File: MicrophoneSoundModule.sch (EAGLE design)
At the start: 23 parts, among them IC1 TLC272 TSSOP8

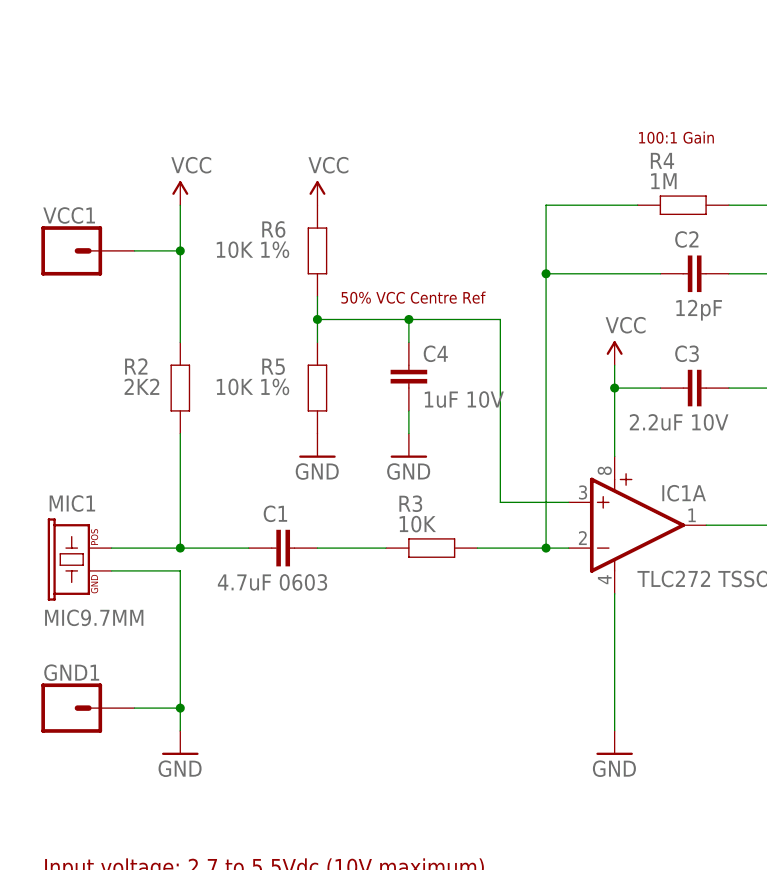
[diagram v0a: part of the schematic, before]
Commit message: Reorient AC decoupling capacitors to reduce noise
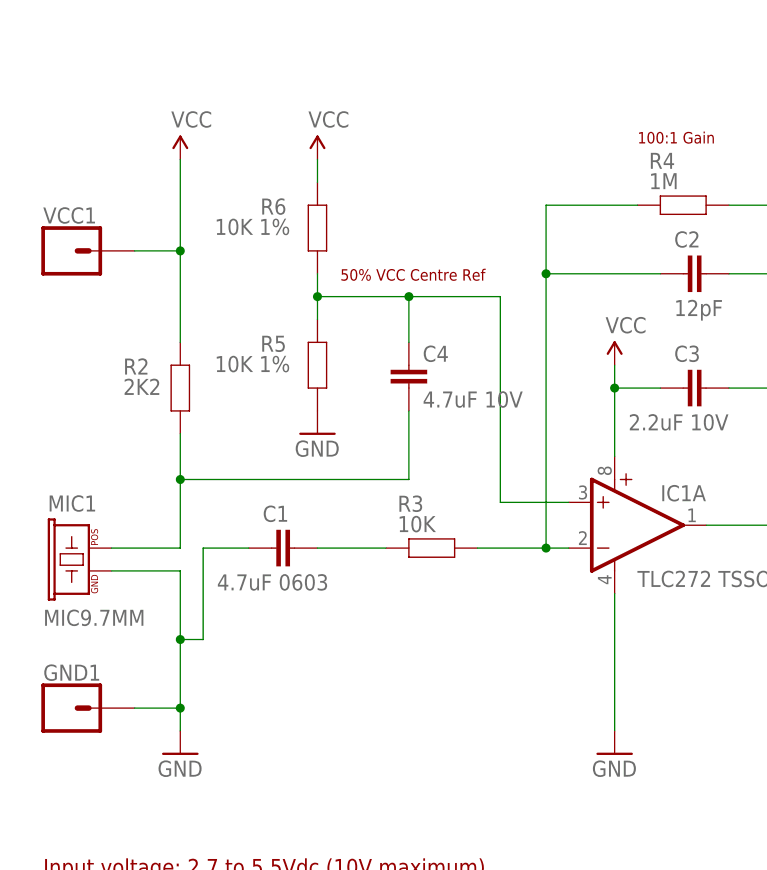
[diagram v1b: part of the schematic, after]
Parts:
- C4: value 1uF 10V -> 4.7uF 10V
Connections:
- net GND: now also C1.1; no longer C4.1
- net N$2: now also C4.1; no longer C1.1
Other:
- moved on the sheet: R5, R6
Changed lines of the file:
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@@
 <part name="R6" library="freetronics-master-v1" deviceset="RESISTOR" device="0603" value="10K 1%"/>
 <part name="P+4" library="freetronics-marc" deviceset="VCC" device=""/>
-<part name="C4" library="freetronics-master-v1" deviceset="CAP" device="0603" value="1uF 10V"/>
-<part name="GND8" library="freetronics" deviceset="GND" device=""/>
+<part name="C4" library="freetronics-master-v1" deviceset="CAP" device="0603" value="4.7uF 10V"/>
 <part name="C5" library="freetronics-master-v1" deviceset="CAP" device="0603" value="100nF"/>
 <part name="R8" library="freetronics-master-v1" deviceset="RESISTOR" device="0603" value="100K"/>
@@
 <text x="68.326" y="14.478" size="1.778" layer="94">www.freetronics.com/mic</text>
 <text x="10.16" y="27.178" size="1.778" layer="94">Input voltage: 2.7 to 5.5Vdc (10V maximum)</text>
-<text x="43.18" y="90.678" size="1.27" layer="94">50% VCC Centre Ref</text>
+<text x="43.18" y="93.218" size="1.27" layer="94">50% VCC Centre Ref</text>
 <text x="76.2" y="108.458" size="1.27" layer="94">100:1 Gain</text>
 <text x="93.98" y="119.888" size="1.6764" layer="94" ratio="10">MIC Output Pin is centred at approx 50% of VCC with no sound</text>
@@
 <attribute name="VALUE" x="80.264" y="89.281" size="1.778" layer="96"/>
 </instance>
-<instance part="P+2" gate="1" x="25.4" y="101.6"/>
+<instance part="P+2" gate="1" x="25.4" y="106.68"/>
 <instance part="C3" gate="G$1" x="83.82" y="81.28" smashed="yes" rot="R90">
 <attribute name="NAME" x="80.264" y="84.201" size="1.778" layer="95"/>
@@
 <instance part="P+3" gate="1" x="73.66" y="83.82"/>
 <instance part="GND3" gate="1" x="73.66" y="40.64"/>
-<instance part="GND4" gate="1" x="40.64" y="73.66"/>
+<instance part="GND4" gate="1" x="40.64" y="76.2"/>
 <instance part="GND6" gate="1" x="93.98" y="78.74"/>
 <instance part="GND7" gate="1" x="25.4" y="40.64"/>
-<instance part="R5" gate="G$1" x="40.64" y="81.28" smashed="yes" rot="R90">
-<attribute name="NAME" x="34.29" y="82.7786" size="1.778" layer="95"/>
-<attribute name="VALUE" x="29.21" y="80.518" size="1.778" layer="96"/>
-</instance>
-<instance part="R6" gate="G$1" x="40.64" y="96.52" smashed="yes" rot="R90">
-<attribute name="NAME" x="34.29" y="98.0186" size="1.778" layer="95"/>
-<attribute name="VALUE" x="29.21" y="95.758" size="1.778" layer="96"/>
-</instance>
-<instance part="P+4" gate="1" x="40.64" y="101.6"/>
+<instance part="R5" gate="G$1" x="40.64" y="83.82" smashed="yes" rot="R90">
+<attribute name="NAME" x="34.29" y="85.3186" size="1.778" layer="95"/>
+<attribute name="VALUE" x="29.21" y="83.058" size="1.778" layer="96"/>
+</instance>
+<instance part="R6" gate="G$1" x="40.64" y="99.06" smashed="yes" rot="R90">
+<attribute name="NAME" x="34.29" y="100.5586" size="1.778" layer="95"/>
+<attribute name="VALUE" x="29.21" y="98.298" size="1.778" layer="96"/>
+</instance>
+<instance part="P+4" gate="1" x="40.64" y="106.68"/>
 <instance part="C4" gate="G$1" x="50.8" y="83.82" smashed="yes" rot="R180">
 <attribute name="NAME" x="52.324" y="84.201" size="1.778" layer="95"/>
 <attribute name="VALUE" x="52.324" y="79.121" size="1.778" layer="96"/>
 </instance>
-<instance part="GND8" gate="1" x="50.8" y="73.66"/>
 <instance part="C5" gate="G$1" x="109.22" y="66.04" smashed="yes" rot="R90">
 <attribute name="NAME" x="105.664" y="68.961" size="1.778" layer="95"/>
@@
 <segment>
 <wire x1="17.78" y1="60.96" x2="25.4" y2="60.96" width="0.1524" layer="91"/>
-<wire x1="25.4" y1="60.96" x2="25.4" y2="45.72" width="0.1524" layer="91"/>
+<wire x1="25.4" y1="60.96" x2="25.4" y2="53.34" width="0.1524" layer="91"/>
+<wire x1="25.4" y1="53.34" x2="25.4" y2="45.72" width="0.1524" layer="91"/>
 <wire x1="25.4" y1="45.72" x2="25.4" y2="43.18" width="0.1524" layer="91"/>
 <wire x1="20.32" y1="45.72" x2="25.4" y2="45.72" width="0.1524" layer="91"/>
@@
 <pinref part="GND7" gate="1" pin="GND"/>
 <pinref part="GND1" gate="G$1" pin="1"/>
+<pinref part="C1" gate="G$1" pin="1"/>
+<wire x1="33.02" y1="63.5" x2="27.94" y2="63.5" width="0.1524" layer="91"/>
+<wire x1="27.94" y1="63.5" x2="27.94" y2="53.34" width="0.1524" layer="91"/>
+<wire x1="27.94" y1="53.34" x2="25.4" y2="53.34" width="0.1524" layer="91"/>
+<junction x="25.4" y="53.34"/>
 </segment>
 <segment>
 <pinref part="GND4" gate="1" pin="GND"/>
 <pinref part="R5" gate="G$1" pin="1"/>
-</segment>
-<segment>
-<wire x1="50.8" y1="78.74" x2="50.8" y2="76.2" width="0.1524" layer="91"/>
-<pinref part="C4" gate="G$1" pin="1"/>
-<pinref part="GND8" gate="1" pin="GND"/>
 </segment>
 <segment>
@@
 <net name="VCC" class="0">
 <segment>
-<wire x1="25.4" y1="101.6" x2="25.4" y2="96.52" width="0.1524" layer="91"/>
+<wire x1="25.4" y1="106.68" x2="25.4" y2="96.52" width="0.1524" layer="91"/>
 <wire x1="25.4" y1="96.52" x2="25.4" y2="86.36" width="0.1524" layer="91"/>
 <wire x1="20.32" y1="96.52" x2="25.4" y2="96.52" width="0.1524" layer="91"/>
@@
 </segment>
 <segment>
-<pinref part="R6" gate="G$1" pin="2"/>
-<pinref part="P+4" gate="1" pin="VCC"/>
-</segment>
-<segment>
 <wire x1="124.46" y1="78.74" x2="124.46" y2="81.28" width="0.1524" layer="91"/>
 <pinref part="R7" gate="G$1" pin="2"/>
 <pinref part="P+5" gate="1" pin="VCC"/>
 </segment>
+<segment>
+<pinref part="P+4" gate="1" pin="VCC"/>
+<pinref part="R6" gate="G$1" pin="2"/>
+<wire x1="40.64" y1="106.68" x2="40.64" y2="104.14" width="0.1524" layer="91"/>
+</segment>
 </net>
 <net name="N$1" class="0">
@@
 <segment>
 <wire x1="17.78" y1="63.5" x2="25.4" y2="63.5" width="0.1524" layer="91"/>
-<wire x1="25.4" y1="63.5" x2="33.02" y2="63.5" width="0.1524" layer="91"/>
-<wire x1="25.4" y1="76.2" x2="25.4" y2="63.5" width="0.1524" layer="91"/>
-<junction x="25.4" y="63.5"/>
+<wire x1="25.4" y1="76.2" x2="25.4" y2="71.12" width="0.1524" layer="91"/>
 <pinref part="MIC1" gate="G$1" pin="POS"/>
-<pinref part="C1" gate="G$1" pin="1"/>
 <pinref part="R2" gate="G$1" pin="1"/>
+<pinref part="C4" gate="G$1" pin="1"/>
+<wire x1="25.4" y1="71.12" x2="25.4" y2="63.5" width="0.1524" layer="91"/>
+<wire x1="50.8" y1="78.74" x2="50.8" y2="71.12" width="0.1524" layer="91"/>
+<wire x1="50.8" y1="71.12" x2="25.4" y2="71.12" width="0.1524" layer="91"/>
+<junction x="25.4" y="71.12"/>
 </segment>
 </net>
@@
 </segment>
 </net>
-<net name="N$5" class="0">
-<segment>
-<wire x1="40.64" y1="91.44" x2="40.64" y2="88.9" width="0.1524" layer="91"/>
-<wire x1="40.64" y1="88.9" x2="40.64" y2="86.36" width="0.1524" layer="91"/>
-<wire x1="50.8" y1="86.36" x2="50.8" y2="88.9" width="0.1524" layer="91"/>
-<wire x1="50.8" y1="88.9" x2="40.64" y2="88.9" width="0.1524" layer="91"/>
-<wire x1="50.8" y1="88.9" x2="60.96" y2="88.9" width="0.1524" layer="91"/>
-<wire x1="60.96" y1="88.9" x2="60.96" y2="68.58" width="0.1524" layer="91"/>
-<wire x1="60.96" y1="68.58" x2="68.58" y2="68.58" width="0.1524" layer="91"/>
-<junction x="40.64" y="88.9"/>
-<junction x="50.8" y="88.9"/>
-<pinref part="R6" gate="G$1" pin="1"/>
-<pinref part="R5" gate="G$1" pin="2"/>
-<pinref part="C4" gate="G$1" pin="2"/>
-<pinref part="IC1" gate="A" pin="+IN"/>
-</segment>
-</net>
 <net name="N$7" class="0">
 <segment>
@@
 </segment>
 </net>
+<net name="N$8" class="0">
+<segment>
+<pinref part="R6" gate="G$1" pin="1"/>
+<wire x1="40.64" y1="93.98" x2="40.64" y2="91.44" width="0.1524" layer="91"/>
+<pinref part="R5" gate="G$1" pin="2"/>
+<wire x1="40.64" y1="91.44" x2="40.64" y2="88.9" width="0.1524" layer="91"/>
+<wire x1="40.64" y1="91.44" x2="50.8" y2="91.44" width="0.1524" layer="91"/>
+<pinref part="C4" gate="G$1" pin="2"/>
+<wire x1="50.8" y1="91.44" x2="50.8" y2="86.36" width="0.1524" layer="91"/>
+<wire x1="50.8" y1="91.44" x2="60.96" y2="91.44" width="0.1524" layer="91"/>
+<wire x1="60.96" y1="91.44" x2="60.96" y2="68.58" width="0.1524" layer="91"/>
+<wire x1="60.96" y1="68.58" x2="68.58" y2="68.58" width="0.1524" layer="91"/>
+<pinref part="IC1" gate="A" pin="+IN"/>
+<junction x="50.8" y="91.44"/>
+<junction x="40.64" y="91.44"/>
+</segment>
+</net>

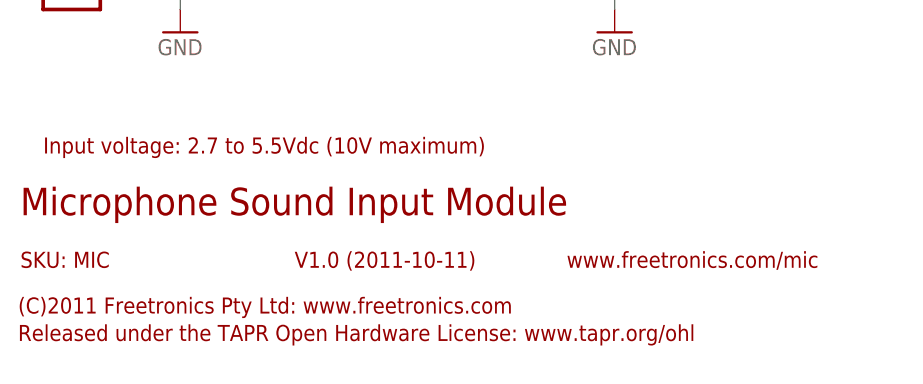
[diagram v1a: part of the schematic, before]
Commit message: Bump revision, add revision to PCB, update schematic PDF
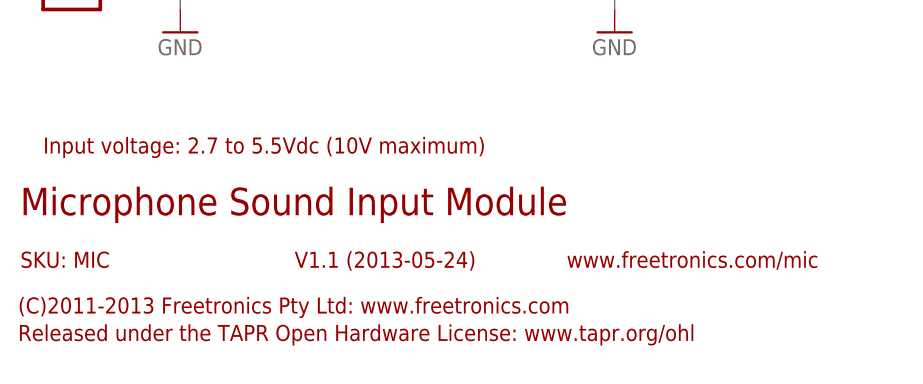
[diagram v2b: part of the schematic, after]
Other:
- note added: "(C)2011-2013 Freetronics Pty Ltd: www.freetronics.com"
- note added: "V1.1 (2013-05-24)"
- note removed: "(C)2011 Freetronics Pty Ltd: www.freetronics.com"
- note removed: "V1.0 (2011-10-11)"
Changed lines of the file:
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@@
 <plain>
 <text x="7.62" y="20.32" size="3.048" layer="94">Microphone Sound Input Module</text>
-<text x="38.1" y="14.478" size="1.778" layer="94">V1.0 (2011-10-11)</text>
+<text x="38.1" y="14.478" size="1.778" layer="94">V1.1 (2013-05-24)</text>
 <text x="7.62" y="14.478" size="1.778" layer="94">SKU: MIC</text>
-<text x="7.366" y="9.398" size="1.778" layer="94">(C)2011 Freetronics Pty Ltd: www.freetronics.com</text>
+<text x="7.366" y="9.398" size="1.778" layer="94">(C)2011-2013 Freetronics Pty Ltd: www.freetronics.com</text>
 <text x="7.366" y="6.35" size="1.778" layer="94">Released under the TAPR Open Hardware License: www.tapr.org/ohl</text>
 <text x="68.326" y="14.478" size="1.778" layer="94">www.freetronics.com/mic</text>
